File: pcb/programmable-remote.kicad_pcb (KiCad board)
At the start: 2 copper layers, 41 parts, among them J1 Conn_01x04_Male, J2 Conn_01x01_Male, Q1 Q_NPN_Darlington_BCE, SW1 SW_Push, SW2 SW_Push, SW3 SW_Push, SW4 SW_Push, SW5 SW_Push, SW6 SW_Push, SW7 SW_Push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

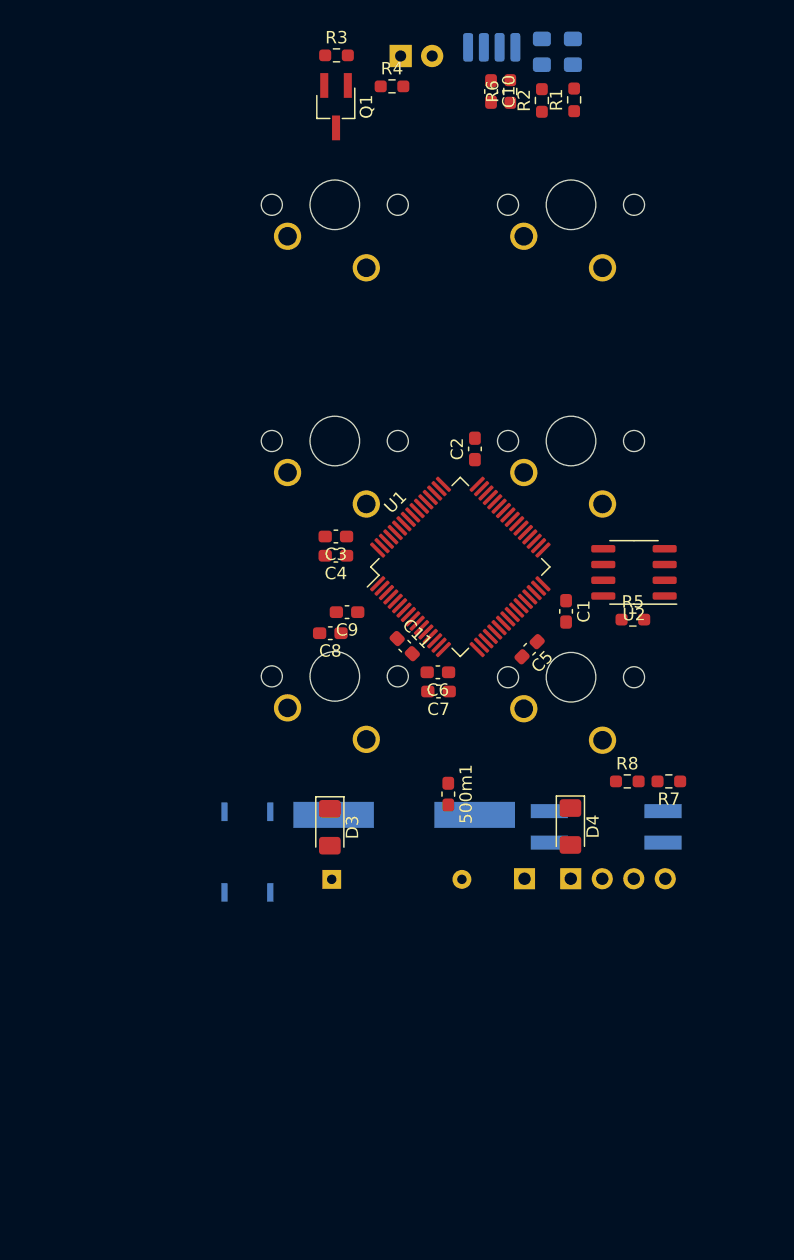
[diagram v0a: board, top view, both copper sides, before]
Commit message: signals routed
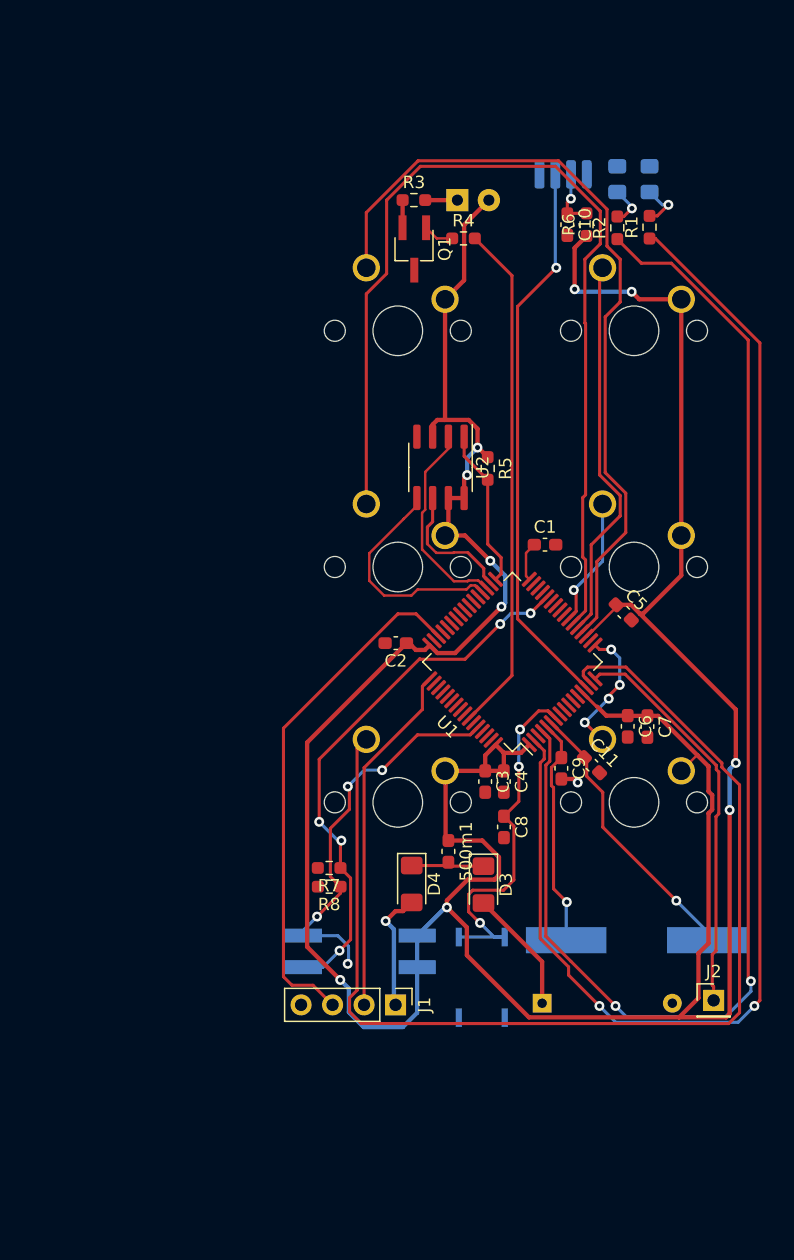
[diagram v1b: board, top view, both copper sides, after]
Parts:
- J1, J2: moved to F.Cu
- moved R7 28.3 mm to (124.5, 120.4)
- moved R8 25.5 mm to (124.5, 121.9), turned to 180 degrees
- moved C3 23.1 mm to (137.1, 113.4), turned to 270 degrees
- moved C4 22.7 mm to (138.6, 113.4), turned to 270 degrees
- moved SW8 22.2 mm to (127.1, 127.1), turned to 90 degrees
- moved SW2 21.4 mm to (136.8, 129.2), turned to 90 degrees
- moved C9 21.4 mm to (143.3, 112.3), turned to 270 degrees
- moved Y1 21.3 mm to (149.3, 126.2)
- moved C8 21.0 mm to (138.6, 117.1), turned to 270 degrees
- moved BT1 19.7 mm to (147.0, 131.3)
- moved J2 18.1 mm to (155.6, 131.1)
- moved C11 17.9 mm to (145.7, 112.1)
- moved U2 17.8 mm to (133.5, 88.1), turned to 270 degrees
- moved J1 17.4 mm to (129.9, 131.4)
- moved C7 17.1 mm to (150.2, 109.0), turned to 270 degrees
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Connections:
- net Net-(BT1-Pad1) renamed /BAT+
- net Net-(D4-Pad2) renamed /SWD_VDD
- net Net-(D5-Pad1) renamed /IR_Pwr2
- net Net-(Q1-Pad2) renamed /IR_Pwr1
- SW1 pad 2: /V3_3 -> VDD
- SW3 pad 2: /V3_3 -> VDD
- SW4 pad 2: /V3_3 -> VDD
- SW5 pad 2: /V3_3 -> VDD
- SW6 pad 2: /V3_3 -> VDD
- SW7 pad 2: /V3_3 -> VDD
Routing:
- net VDD: track 0.00 -> 283.9 mm, vias 0 -> 10
- net /STATUS: track 0.00 -> 103.5 mm, vias 0 -> 2
- net /FAIL: track 0.00 -> 103.5 mm, vias 0 -> 2
- net /KESC: track 0.00 -> 91.6 mm
- net /K2: track 0.00 -> 79.4 mm
- net /K0: track 0.00 -> 64.4 mm
- net /IR_IN: track 0.00 -> 45.0 mm, vias 0 -> 1
- net /BOOT1: track 0.00 -> 44.4 mm, vias 0 -> 5
- net /SWDIO: track 0.00 -> 42.0 mm
- net /IR_OUT: track 0.00 -> 41.4 mm
- net /USART_TX: track 0.00 -> 32.3 mm
- net /BOOT0: track 0.00 -> 32.2 mm, vias 0 -> 4
- net /K1: track 0.00 -> 31.2 mm
- net /NRST: track 0.00 -> 30.6 mm, vias 0 -> 3
- net /SWCLK: track 0.00 -> 28.5 mm
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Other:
- net class Default: clearance 0.3 -> 0.2
- net class Pwr added: clearance 0.2, trace_width 0.35, via_dia 0.8, via_drill 0.4
- rule trace_clearance: 0.3 -> 0.2

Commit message: ground pour added
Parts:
- moved C6 13.2 mm to (138.4, 117.3)
- moved J2 13.2 mm to (145.3, 139.4)
- moved R5 13.2 mm to (127.1, 96.5)
- moved C11 13.2 mm to (135.5, 120.4)
- moved C7 13.2 mm to (140.0, 117.3)
- moved C9 13.2 mm to (133.1, 120.6)
- moved R6 13.2 mm to (135.1, 76.8)
- moved SW3 13.2 mm to (136.4, 118.3)
- moved SW5 13.2 mm to (136.4, 80.3)
- moved SW7 13.2 mm to (136.4, 99.3)
- moved D3 13.2 mm to (126.8, 130.0)
- moved J1 13.2 mm to (119.7, 139.7)
- moved Q1 13.2 mm to (121.2, 78.8)
- moved R7 13.2 mm to (114.3, 128.7)
- moved 500m1 13.2 mm to (124.0, 127.3)
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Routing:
- net VDD: track 283.9 -> 305.8 mm
- net GND: track 1.44 -> 19.3 mm, vias 1 -> 45
- added copper zone on B.Cu, net GND
- added copper zone on F.Cu, net GND
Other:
- board outline added: 42 x 72.2 mm

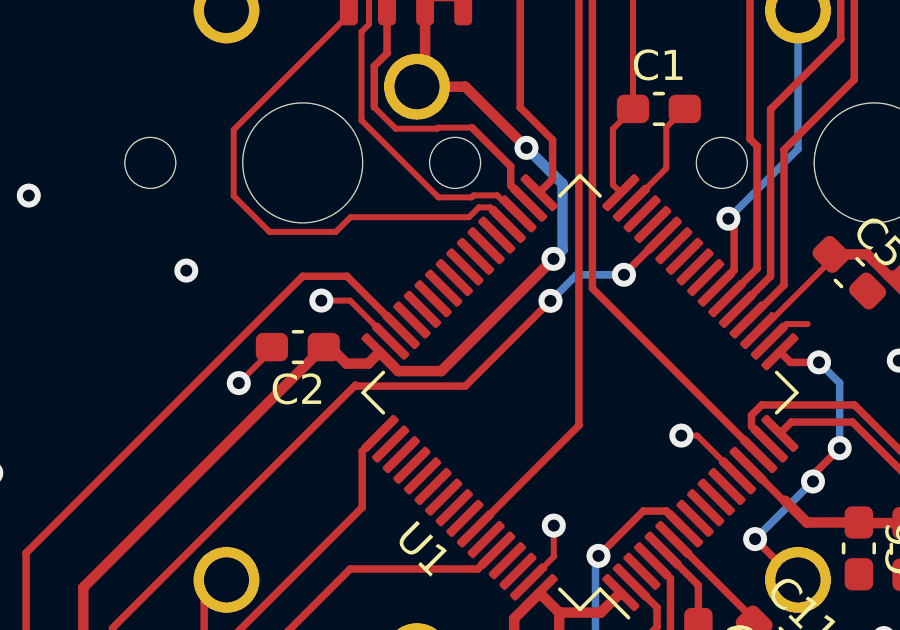
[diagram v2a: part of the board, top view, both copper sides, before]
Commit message: ground pour added
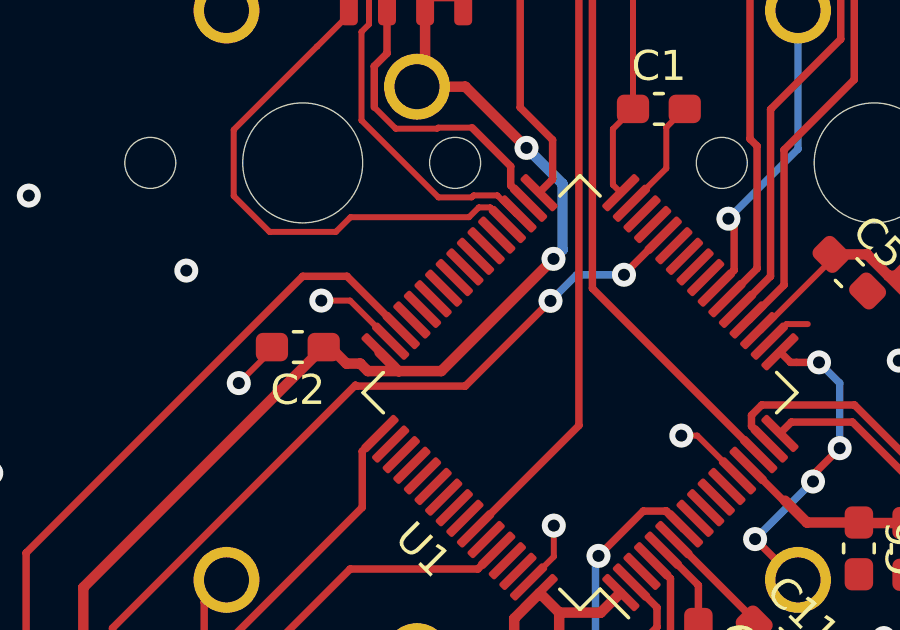
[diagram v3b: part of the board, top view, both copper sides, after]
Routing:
- net VDD: track 305.8 -> 306.4 mm
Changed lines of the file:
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@@
     (thickness 1.6)
     (drawings 8)
-    (tracks 495)
+    (tracks 497)
     (zones 0)
     (modules 41)
@@
   (segment (start 130.457999 140.727001) (end 142.565761 140.727001) (width 0.35) (layer F.Cu) (net 2))
   (segment (start 140.865 116.415) (end 140.01 116.415) (width 0.35) (layer F.Cu) (net 2))
-  (segment (start 120.58 110.55) (end 120.8 110.55) (width 0.35) (layer F.Cu) (net 2))
-  (segment (start 120.956318 110.706318) (end 120.956318 110.716318) (width 0.35) (layer F.Cu) (net 2))
-  (segment (start 120.8 110.55) (end 120.956318 110.706318) (width 0.35) (layer F.Cu) (net 2))
-  (segment (start 120.956318 110.716318) (end 121.34 111.1) (width 0.35) (layer F.Cu) (net 2))
-  (segment (start 122.064998 111.1) (end 122.440994 110.724004) (width 0.35) (layer F.Cu) (net 2))
-  (segment (start 121.34 111.1) (end 122.064998 111.1) (width 0.35) (layer F.Cu) (net 2))
   (segment (start 138.692098 107.46) (end 137.49 107.46) (width 0.35) (layer F.Cu) (net 2))
   (segment (start 139.406049 108.173951) (end 139.656049 108.173951) (width 0.35) (layer F.Cu) (net 2))
@@
   (segment (start 128.54 107.31) (end 128.24 107.61) (width 0.35) (layer B.Cu) (net 2))
   (segment (start 128.54 105.11) (end 128.54 107.31) (width 0.35) (layer B.Cu) (net 2))
-  (segment (start 123.067773 111.350783) (end 122.440994 110.724004) (width 0.35) (layer F.Cu) (net 2))
-  (segment (start 124.499217 111.350783) (end 123.067773 111.350783) (width 0.35) (layer F.Cu) (net 2))
-  (segment (start 128.24 107.61) (end 124.499217 111.350783) (width 0.35) (layer F.Cu) (net 2))
   (segment (start 121.44 140.355002) (end 120.285002 141.51) (width 0.35) (layer B.Cu) (net 2))
   (segment (start 121.44 136.68) (end 121.44 140.355002) (width 0.35) (layer B.Cu) (net 2))
@@
   (segment (start 130.89 85.26) (end 134.14 82.01) (width 0.2) (layer F.Cu) (net 2))
   (segment (start 130.89 102.61) (end 130.89 85.26) (width 0.2) (layer F.Cu) (net 2))
+  (segment (start 121.8 111.1) (end 122.050783 111.350783) (width 0.35) (layer F.Cu) (net 2))
+  (segment (start 121.34 111.1) (end 121.8 111.1) (width 0.35) (layer F.Cu) (net 2))
+  (segment (start 120.956318 110.706318) (end 120.956318 110.716318) (width 0.35) (layer F.Cu) (net 2))
+  (segment (start 120.956318 110.716318) (end 121.34 111.1) (width 0.35) (layer F.Cu) (net 2))
+  (segment (start 120.8 110.55) (end 120.956318 110.706318) (width 0.35) (layer F.Cu) (net 2))
+  (segment (start 124.499217 111.350783) (end 128.24 107.61) (width 0.35) (layer F.Cu) (net 2))
+  (segment (start 120.58 110.55) (end 120.8 110.55) (width 0.35) (layer F.Cu) (net 2))
+  (segment (start 123.067773 111.350783) (end 122.440994 110.724004) (width 0.35) (layer F.Cu) (net 2))
+  (segment (start 123.100783 111.350783) (end 123.067773 111.350783) (width 0.35) (layer F.Cu) (net 2))
+  (segment (start 122.050783 111.350783) (end 123.100783 111.350783) (width 0.35) (layer F.Cu) (net 2))
+  (segment (start 123.100783 111.350783) (end 124.499217 111.350783) (width 0.35) (layer F.Cu) (net 2))
   (via (at 134.39 121.79) (size 0.8) (drill 0.4) (layers F.Cu B.Cu) (net 3))
   (segment (start 134.105 121.505) (end 134.39 121.79) (width 0.35) (layer F.Cu) (net 3))

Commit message: Pcb 1.0
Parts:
- added TP1: TestPoint, programmable-remote:TestPoint_harwin_S2761-46R, F.Cu at (124.7, 72.8)
- added TP2: TestPoint, programmable-remote:TestPoint_harwin_S2761-46R, F.Cu at (124.0, 77.5)
- added TP3: TestPoint, programmable-remote:TestPoint_harwin_S2761-46R, F.Cu at (116.8, 102.2)
- added TP4: TestPoint, programmable-remote:TestPoint_harwin_S2761-46R, F.Cu at (120.9, 100.8)
- added TP5: TestPoint, programmable-remote:TestPoint_harwin_S2761-46R, F.Cu at (122.7, 99.2)
- added TP6: TestPoint, programmable-remote:TestPoint_harwin_S2761-46R, F.Cu at (126.8, 99.2)
- added TP7: TestPoint, programmable-remote:TestPoint_harwin_S2761-46R, F.Cu at (133.7, 94.2)
- added TP8: TestPoint, programmable-remote:TestPoint_harwin_S2761-46R, F.Cu at (128.9, 128.5)
- J2: moved to B.Cu
- moved U2 2.75 mm to (123.3, 93.6)
- moved R4 1.49 mm to (126.7, 77.9)
- moved R5 1.21 mm to (127.2, 95.2)
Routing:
- net /KESC: track 91.6 -> 24.5 mm, vias 0 -> 4
- net VDD: track 306.4 -> 321.7 mm, vias 10 -> 8
- net /MOSI: track 18.4 -> 24.1 mm
- net /CS: track 12.9 -> 17.1 mm
- net /MISO: track 16.5 -> 20.5 mm
- net /BOOT1: track 44.4 -> 47.6 mm
- net /SCK: track 10.8 -> 13.8 mm
- net /SWCLK: track 28.5 -> 31.5 mm
- net GND: track 19.3 -> 16.6 mm, vias 45 -> 61
- net /K2: track 79.4 -> 81.7 mm
- net /IR_Pwr2: track 2.59 -> 4.63 mm
- net /K0: track 64.4 -> 66.3 mm
- net /USART_TX: track 32.3 -> 34.0 mm
- net Net-(Q1-Pad1): track 2.46 -> 3.94 mm
- net /KOK: track 10.8 -> 12.2 mm
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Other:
- net class Default: trace_width 0.25 -> 0.2
- rule pad_to_mask_clearance: 0 -> 0.05
